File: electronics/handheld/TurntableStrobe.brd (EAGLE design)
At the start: 25.1 x 17.8 mm, 18 parts, among them IC1 TINY25, J1 ISP, Q1 12MHz

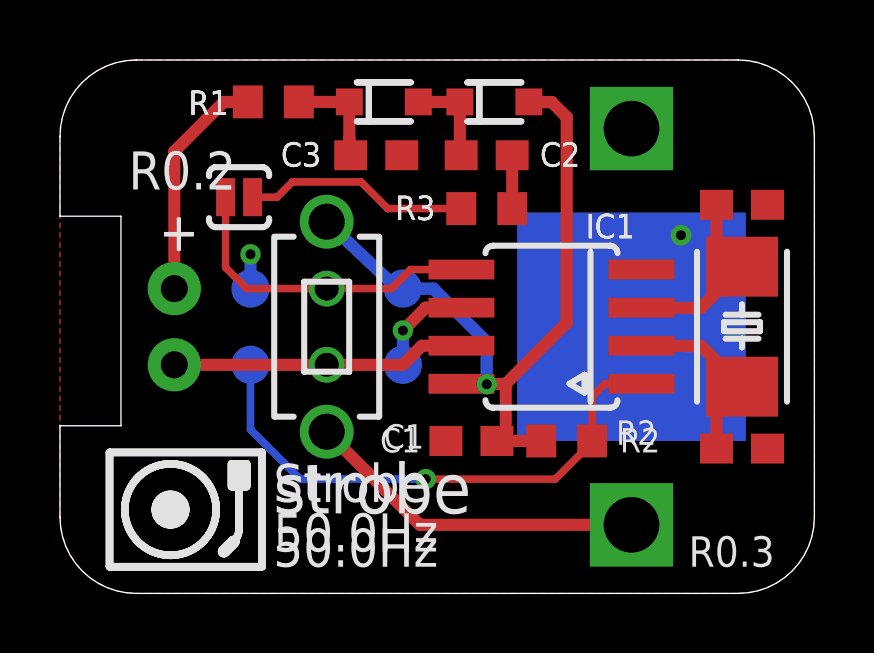
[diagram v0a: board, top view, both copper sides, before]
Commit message: Prototype LM2665 charge pump
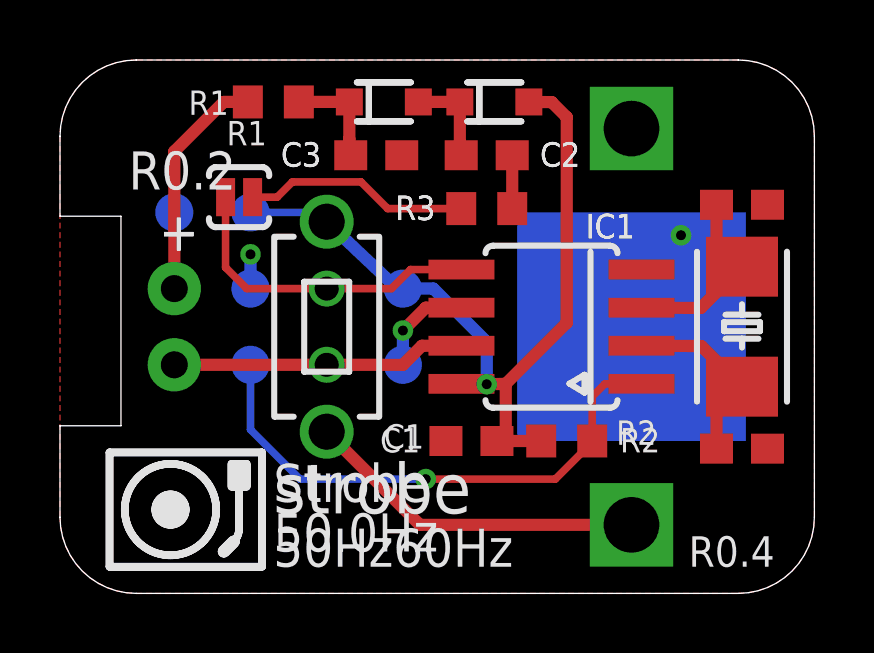
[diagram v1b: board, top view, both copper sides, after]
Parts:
- added TP1: VCC, SparkFun-Connectors:PAD.03X.05
- added TP2: LED, SparkFun-Connectors:PAD.03X.05
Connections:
- net N$3: now also TP2.P$1
- net VCC: now also TP1.P$1
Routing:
- net VCC: track 24.6 -> 27.3 mm
- net N$3: track 7.71 -> 10.2 mm
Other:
- board text added: "50Hz60Hz"
- board text added: "R0.4"
- board text removed: "R0.3"
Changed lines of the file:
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@@
 <layer number="112" name="tSilk" color="7" fill="1" visible="no" active="yes"/>
 <layer number="113" name="IDFDebug" color="4" fill="1" visible="no" active="yes"/>
+<layer number="114" name="Badge_Outline" color="7" fill="1" visible="yes" active="yes"/>
+<layer number="115" name="ReferenceISLANDS" color="7" fill="1" visible="yes" active="yes"/>
 <layer number="116" name="Patch_BOT" color="9" fill="4" visible="no" active="yes"/>
+<layer number="118" name="Rect_Pads" color="7" fill="1" visible="yes" active="yes"/>
 <layer number="121" name="tsilk" color="14" fill="1" visible="no" active="yes"/>
 <layer number="122" name="bsilk" color="6" fill="1" visible="no" active="yes"/>
@@
 <wire x1="2.032" y1="12.573" x2="2.032" y2="5.588" width="0" layer="20"/>
 <wire x1="2.032" y1="5.588" x2="0" y2="5.588" width="0" layer="20"/>
-<text x="20.955" y="0.889" size="1.016" layer="25" font="vector" ratio="10">R0.3</text>
+<text x="20.955" y="0.889" size="1.016" layer="25" font="vector" ratio="10">R0.4</text>
 <circle x="3.683" y="2.794" radius="1.524" width="0.254" layer="21"/>
 <polygon width="0.254" layer="21">
@@
 <vertex x="5.715" y="3.556"/>
 </polygon>
-<text x="7.112" y="0.889" size="1.27" layer="25" font="vector" ratio="10">50.0Hz</text>
+<text x="7.112" y="0.889" size="1.27" layer="25" font="vector" ratio="10">50Hz60Hz</text>
 <wire x1="5.969" y1="3.937" x2="5.969" y2="2.159" width="0.254" layer="121"/>
 <wire x1="5.789396875" y1="1.725396875" x2="5.969" y2="2.159" width="0.254" layer="121" curve="45"/>
@@
 <elements>
 <element name="R1" library="rcl" package="R0603" value="1K" x="7.112" y="16.383" smashed="yes" rot="R180">
-<attribute name="NAME" x="5.621" y="16.764" size="0.8128" layer="25" font="vector" ratio="10" rot="R180"/>
+<attribute name="NAME" x="6.891" y="15.748" size="0.8128" layer="25" font="vector" ratio="10" rot="R180"/>
 </element>
 <element name="R2" library="rcl" package="R0603" value="10K" x="16.891" y="5.08" smashed="yes">
@@
 </element>
 <element name="U$5" library="bt" package="BTLOGOM" value="BTLOGO-LOGO-MD" x="5.334" y="1.524" rot="MR0"/>
+<element name="TP1" library="SparkFun-Connectors" package="PAD.03X.05" value="VCC" x="6.35" y="12.7" rot="MR90"/>
+<element name="TP2" library="SparkFun-Connectors" package="PAD.03X.05" value="LED" x="3.81" y="12.7" rot="MR90"/>
 </elements>
 <signals>
@@
 <wire x1="14.224" y1="8.382" x2="14.224" y2="6.9723" width="0.4064" layer="16"/>
 <via x="14.224" y="6.9723" extent="1-16" drill="0.3302"/>
+<contactref element="TP1" pad="P$1"/>
+<wire x1="6.35" y1="12.7" x2="8.58" y2="12.7" width="0.254" layer="16"/>
+<wire x1="8.58" y1="12.7" x2="8.89" y2="12.39" width="0.254" layer="16"/>
 </signal>
 <signal name="GND">
@@
 <wire x1="5.461" y1="16.383" x2="3.81" y2="14.732" width="0.4064" layer="1"/>
 <wire x1="3.81" y1="14.732" x2="3.81" y2="10.16" width="0.4064" layer="1"/>
+<contactref element="TP2" pad="P$1"/>
+<wire x1="3.81" y1="12.7" x2="3.81" y2="10.16" width="0.254" layer="16"/>
 </signal>
 <signal name="VHI">
